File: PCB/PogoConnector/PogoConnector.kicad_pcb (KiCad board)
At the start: 2 copper layers, 7 x 20 mm, 7 parts, among them J1 PogoPinPad, J2 Conn_01x06, J3 PogoPinPad, J4 PogoPinPad, U1 PogoPin, U2 PogoPin, U3 PogoPin

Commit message: Update PCB
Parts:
- J2: footprint Connector_PinHeader_2.54mm:PinHeader_1x06_P2.54mm_Vertical -> CustomFootprints:Connector_PinHeader_2.54mm_Vertical
- moved J2 6.35 mm to (126.8, 95.0)
- moved J1 0.23 mm to (129.8, 96.5)
- moved J3 0.23 mm to (129.8, 99.5)
- moved J4 0.23 mm to (129.8, 102.5)
- moved U1 0.23 mm to (129.8, 87.5)
- moved U2 0.23 mm to (129.8, 90.5)
- moved U3 0.23 mm to (129.8, 93.5)
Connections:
- J1 pad 1: /Data1 -> GND
- J2 pad 1: GND -> +5V
- J2 pad 2: +5V -> /Data1
- J2 pad 3: /Data2 -> GND
- J2 pad 4: /Data1 -> GND
- J2 pad 5: +5V -> /Data2
- J2 pad 6: GND -> +5V
- J3 pad 1: +5V -> /Data2
- J4 pad 1: GND -> +5V
- U1 pad 1: GND -> +5V
- U2 pad 1: +5V -> /Data1
- U3 pad 1: /Data2 -> GND
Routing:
- net GND: track 7.45 -> 6.39 mm
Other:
- outline, holes or cut-outs redrawn

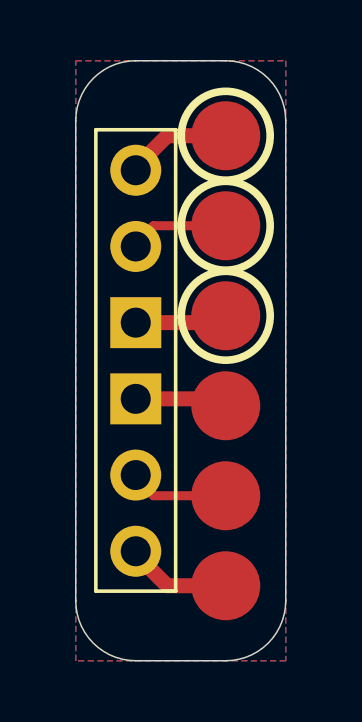
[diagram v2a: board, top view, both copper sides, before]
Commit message: Add hall sensor shield
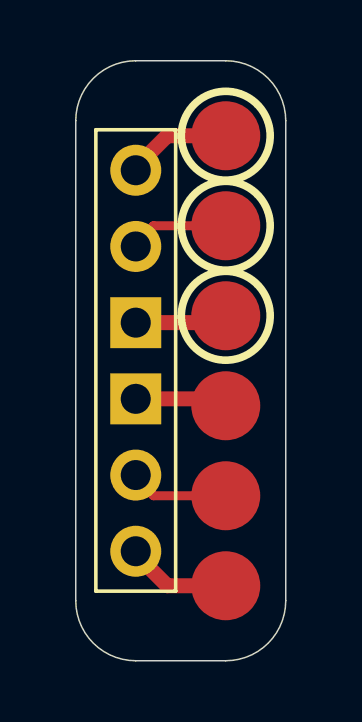
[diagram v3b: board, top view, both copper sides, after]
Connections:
- J1 pad 1: GND -> GND2
- J2 pad 4: GND -> GND2
- J2 pad 6: +5V -> +5V2
- J4 pad 1: +5V -> +5V2
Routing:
- net +5V2: track 0.00 -> 3.58 mm
- net +5V: track 7.15 -> 3.58 mm
- net GND: track 6.39 -> 3.20 mm
- net GND2: track 0.00 -> 3.20 mm
- removed copper zone on F.Cu, net +5V
- removed copper zone on B.Cu, net GND
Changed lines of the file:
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@@
 	(net 3 "/Data2")
 	(net 4 "+5V")
+	(net 5 "GND2")
+	(net 6 "+5V2")
 	(footprint "CustomFootprints:Connector_PinHeader_2.54mm_Vertical"
 		(layer "F.Cu")
@@
 			)
 			(remove_unused_layers no)
-			(net 1 "GND")
+			(net 5 "GND2")
 			(pinfunction "Pin_4")
 			(pintype "passive")
@@
 			)
 			(remove_unused_layers no)
-			(net 4 "+5V")
+			(net 6 "+5V2")
 			(pinfunction "Pin_6")
 			(pintype "passive")
@@
 			(size 2.3 2.3)
 			(layers "F.Cu" "F.Paste" "F.Mask")
-			(net 1 "GND")
+			(net 5 "GND2")
 			(pinfunction "Pin_1")
 			(pintype "passive")
@@
 			(size 2.3 2.3)
 			(layers "F.Cu" "F.Paste" "F.Mask")
-			(net 4 "+5V")
+			(net 6 "+5V2")
 			(pinfunction "Pin_1")
 			(pintype "passive")
@@
 	)
 	(segment
+		(start 127.36 90.5)
+		(end 126.67 91.19)
+		(width 0.3)
+		(layer "F.Cu")
+		(net 2)
+	)
+	(segment
+		(start 129.77 90.5)
+		(end 127.36 90.5)
+		(width 0.3)
+		(layer "F.Cu")
+		(net 2)
+	)
+	(segment
+		(start 129.77 99.5)
+		(end 127.36 99.5)
+		(width 0.3)
+		(layer "F.Cu")
+		(net 3)
+	)
+	(segment
+		(start 127.36 99.5)
+		(end 126.67 98.81)
+		(width 0.3)
+		(layer "F.Cu")
+		(net 3)
+	)
+	(segment
+		(start 129.77 87.5)
+		(end 127.82 87.5)
+		(width 0.5)
+		(layer "F.Cu")
+		(net 4)
+	)
+	(segment
+		(start 127.82 87.5)
+		(end 126.67 88.65)
+		(width 0.5)
+		(layer "F.Cu")
+		(net 4)
+	)
+	(segment
 		(start 126.67 96.27)
 		(end 129.54 96.27)
 		(width 0.5)
 		(layer "F.Cu")
-		(net 1)
+		(net 5)
 	)
 	(segment
@@
 		(width 0.5)
 		(layer "F.Cu")
-		(net 1)
-	)
-	(segment
-		(start 127.36 90.5)
-		(end 126.67 91.19)
-		(width 0.3)
-		(layer "F.Cu")
-		(net 2)
-	)
-	(segment
-		(start 129.77 90.5)
-		(end 127.36 90.5)
-		(width 0.3)
-		(layer "F.Cu")
-		(net 2)
-	)
-	(segment
-		(start 129.77 99.5)
-		(end 127.36 99.5)
-		(width 0.3)
-		(layer "F.Cu")
-		(net 3)
-	)
-	(segment
-		(start 127.36 99.5)
-		(end 126.67 98.81)
-		(width 0.3)
-		(layer "F.Cu")
-		(net 3)
+		(net 5)
 	)
 	(segment
@@
 		(width 0.5)
 		(layer "F.Cu")
-		(net 4)
-	)
-	(segment
-		(start 129.77 87.5)
-		(end 127.82 87.5)
-		(width 0.5)
-		(layer "F.Cu")
-		(net 4)
-	)
-	(segment
-		(start 127.82 87.5)
-		(end 126.67 88.65)
-		(width 0.5)
-		(layer "F.Cu")
-		(net 4)
+		(net 6)
 	)
 	(segment
@@
 		(width 0.5)
 		(layer "F.Cu")
-		(net 4)
-	)
-	(zone
-		(net 4)
-		(net_name "+5V")
-		(layer "F.Cu")
-		(hatch edge 0.5)
-		(connect_pads yes
-			(clearance 0.5)
-		)
-		(min_thickness 0.25)
-		(filled_areas_thickness no)
-		(fill yes
-			(thermal_gap 0.5)
-			(thermal_bridge_width 0.5)
-		)
-		(polygon
-			(pts
-				(xy 124.77 85) (xy 131.77 85) (xy 131.77 105) (xy 124.77 105)
-			)
-		)
-	)
-	(zone
-		(net 1)
-		(net_name "GND")
-		(layer "B.Cu")
-		(hatch edge 0.5)
-		(priority 1)
-		(connect_pads yes
-			(clearance 0.5)
-		)
-		(min_thickness 0.25)
-		(filled_areas_thickness no)
-		(fill yes
-			(thermal_gap 0.5)
-			(thermal_bridge_width 0.5)
-		)
-		(polygon
-			(pts
-				(xy 124.77 85) (xy 131.77 85) (xy 131.77 105) (xy 124.77 105)
-			)
-		)
+		(net 6)
 	)
 )

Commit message: Add smart cube panel
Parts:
- added REF**: Tab, PCM_kikit:Tab, F.Cu at (124.6, 95.0)
- added REF**: Tab, PCM_kikit:Tab, F.Cu at (132.0, 95.0)
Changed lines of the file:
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@@
 	(net 5 "GND2")
 	(net 6 "+5V2")
+	(footprint "PCM_kikit:Tab"
+		(layer "F.Cu")
+		(at 124.57 95)
+		(descr "A symbol representing annotation for tab placement")
+		(property "Reference" "REF**"
+			(at -0.25 -2 0)
+			(layer "F.SilkS")
+			(hide yes)
+			(effects
+				(font
+					(size 1 1)
+					(thickness 0.15)
+				)
+			)
+		)
+		(property "Value" "Tab"
+			(at -3 -1 0)
+			(layer "Dwgs.User")
+			(effects
+				(font
+					(size 1.2 1.2)
+					(thickness 0.2)
+				)
+			)
+		)
+		(property "Footprint" "PCM_kikit:Tab"
+			(at 0 0 0)
+			(layer "F.Fab")
+			(hide yes)
+			(effects
+				(font
+					(size 1.27 1.27)
+					(thickness 0.15)
+				)
+			)
+		)
+		(property "Datasheet" ""
+			(at 0 0 0)
+			(layer "F.Fab")
+			(hide yes)
+			(effects
+				(font
+					(size 1.27 1.27)
+					(thickness 0.15)
+				)
+			)
+		)
+		(property "Description" ""
+			(at 0 0 0)
+			(layer "F.Fab")
+			(hide yes)
+			(effects
+				(font
+					(size 1.27 1.27)
+					(thickness 0.15)
+				)
+			)
+		)
+		(attr board_only exclude_from_pos_files exclude_from_bom allow_missing_courtyard)
+		(fp_line
+			(start 0 0)
+			(end -3 0)
+			(stroke
+				(width 0.3)
+				(type solid)
+			)
+			(layer "Dwgs.User")
+		)
+		(fp_line
+			(start 0 0)
+			(end -1 -1)
+			(stroke
+				(width 0.3)
+				(type solid)
+			)
+			(layer "Dwgs.User")
+		)
+		(fp_line
+			(start 0 0)
+			(end -1 1)
+			(stroke
+				(width 0.3)
+				(type solid)
+			)
+			(layer "Dwgs.User")
+		)
+		(fp_line
+			(start 0 1)
+			(end 0 -1)
+			(stroke
+				(width 0.3)
+				(type solid)
+			)
+			(layer "Dwgs.User")
+		)
+		(fp_text user "KIKIT: width: 5mm"
+			(at -5.5 0 90)
+			(layer "Dwgs.User")
+			(effects
+				(font
+					(size 1 1)
+					(thickness 0.15)
+				)
+			)
+		)
+	)
 	(footprint "CustomFootprints:Connector_PinHeader_2.54mm_Vertical"
 		(layer "F.Cu")
@@
 			)
 		)
+	)
+	(footprint "PCM_kikit:Tab"
+		(layer "F.Cu")
+		(at 131.97 95 180)
+		(descr "A symbol representing annotation for tab placement")
+		(property "Reference" "REF**"
+			(at -0.25 -2 0)
+			(layer "F.SilkS")
+			(hide yes)
+			(effects
+				(font
+					(size 1 1)
+					(thickness 0.15)
+				)
+			)
+		)
+		(property "Value" "Tab"
+			(at -3 -1 0)
+			(layer "Dwgs.User")
+			(effects
+				(font
+					(size 1.2 1.2)
+					(thickness 0.2)
+				)
+			)
+		)
+		(property "Footprint" "PCM_kikit:Tab"
+			(at 0 0 0)
+			(layer "F.Fab")
+			(hide yes)
+			(effects
+				(font
+					(size 1.27 1.27)
+					(thickness 0.15)
+				)
+			)
+		)
+		(property "Datasheet" ""
+			(at 0 0 0)
+			(layer "F.Fab")
+			(hide yes)
+			(effects
+				(font
+					(size 1.27 1.27)
+					(thickness 0.15)
+				)
+			)
+		)
+		(property "Description" ""
+			(at 0 0 0)
+			(layer "F.Fab")
+			(hide yes)
+			(effects
+				(font
+					(size 1.27 1.27)
+					(thickness 0.15)
+				)
+			)
+		)
+		(attr board_only exclude_from_pos_files exclude_from_bom allow_missing_courtyard)
+		(fp_line
+			(start 0 1)
+			(end 0 -1)
+			(stroke
+				(width 0.3)
+				(type solid)
+			)
+			(layer "Dwgs.User")
+		)
+		(fp_line
+			(start 0 0)
+			(end -1 1)
+			(stroke
+				(width 0.3)
+				(type solid)
+			)
+			(layer "Dwgs.User")
+		)
+		(fp_line
+			(start 0 0)
+			(end -1 -1)
+			(stroke
+				(width 0.3)
+				(type solid)
+			)
+			(layer "Dwgs.User")
+		)
+		(fp_line
+			(start 0 0)
+			(end -3 0)
+			(stroke
+				(width 0.3)
+				(type solid)
+			)
+			(layer "Dwgs.User")
+		)
+		(fp_text user "KIKIT: width: 5mm"
+			(at -5.5 0 90)
+			(layer "Dwgs.User")
+			(effects
+				(font
+					(size 1 1)
+					(thickness 0.15)
+				)
+			)
+		)

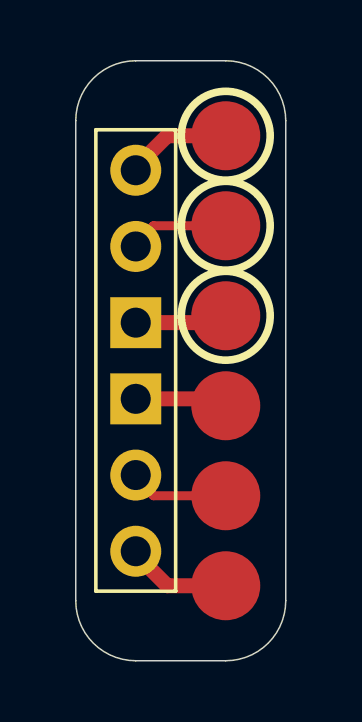
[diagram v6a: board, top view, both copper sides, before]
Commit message: Finish module, power supply and connector design, panel is wip
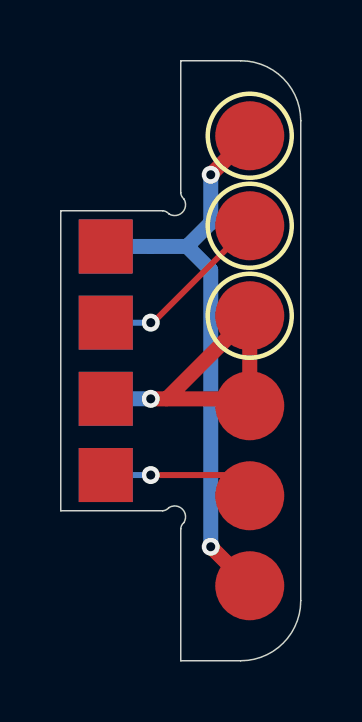
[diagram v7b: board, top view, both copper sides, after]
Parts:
- J2: footprint CustomFootprints:Connector_PinHeader_2.54mm_Vertical -> CustomFootprints:01x04_PinPads; moved to B.Cu
- moved J2 1.00 mm to (125.8, 95.0), turned to -90 degrees
- moved J1 0.80 mm to (130.6, 96.5)
- moved J3 0.80 mm to (130.6, 99.5)
- moved J4 0.80 mm to (130.6, 102.5)
- moved U1 0.80 mm to (130.6, 87.5)
- moved U2 0.80 mm to (130.6, 90.5)
- moved U3 0.80 mm to (130.6, 93.5)
- moved REF** 0.50 mm to (124.1, 95.0)
- moved REF** 0.50 mm to (132.5, 95.0)
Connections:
- J1 pad 1: GND2 -> GND
- J2 pad 4: GND2 -> /Data2
- J4 pad 1: +5V2 -> +5V
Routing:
- net +5V: track 3.58 -> 19.4 mm, vias 0 -> 2
- net GND: track 3.20 -> 11.8 mm, vias 0 -> 1
- net +5V2: track 3.58 -> 0.00 mm
- net GND2: track 3.20 -> 0.00 mm
- net /Data1: track 3.39 -> 6.14 mm, vias 0 -> 1
- net /Data2: track 3.39 -> 5.09 mm, vias 0 -> 1
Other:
- board size 7 x 20 mm -> 8 x 20 mm
- board text added: "+"
- board text added: "-"
- board text added: "1"
- board text added: "2"
- board text added: "5V"
- board text added: "D1"
- board text added: "D2"
- board text added: "GND"

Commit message: Finish panel script
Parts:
- added J5: Conn_01x06, CustomFootprints:01x04_PinPads_Single, B.Cu at (129.2, 95.0)
- J2: footprint CustomFootprints:01x04_PinPads -> CustomFootprints:01x04_PinPads_Single
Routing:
- net GND: track 11.8 -> 12.7 mm
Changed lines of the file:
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@@
 		)
 	)
-	(footprint "CustomFootprints:01x04_PinPads"
+	(footprint "CustomFootprints:01x04_PinPads_Single"
+		(layer "B.Cu")
+		(at 129.17 95 -90)
+		(property "Reference" "J5"
+			(at 0 0.5 90)
+			(unlocked yes)
+			(layer "B.SilkS")
+			(hide yes)
+			(effects
+				(font
+					(size 1 1)
+					(thickness 0.1)
+				)
+				(justify mirror)
+			)
+		)
+		(property "Value" "Conn_01x06"
+			(at 0 -1 90)
+			(unlocked yes)
+			(layer "B.Fab")
+			(effects
+				(font
+					(size 1 1)
+					(thickness 0.15)
+				)
+				(justify mirror)
+			)
+		)
+		(property "Footprint" "CustomFootprints:01x04_PinPads_Single"
+			(at 0 0 90)
+			(unlocked yes)
+			(layer "B.Fab")
+			(hide yes)
+			(effects
+				(font
+					(size 1 1)
+					(thickness 0.15)
+				)
+				(justify mirror)
+			)
+		)
+		(property "Datasheet" ""
+			(at 0 0 90)
+			(unlocked yes)
+			(layer "B.Fab")
+			(hide yes)
+			(effects
+				(font
+					(size 1 1)
+					(thickness 0.15)
+				)
+				(justify mirror)
+			)
+		)
+		(property "Description" "Generic connector, single row, 01x04, script generated (kicad-library-utils/schlib/autogen/connector/)"
+			(at 0 0 90)
+			(unlocked yes)
+			(layer "B.Fab")
+			(hide yes)
+			(effects
+				(font
+					(size 1 1)
+					(thickness 0.15)
+				)
+				(justify mirror)
+			)
+		)
+		(property ki_fp_filters "Connector*:*_1x??_*")
+		(sheetname "Root")
+		(sheetfile "PogoConnector.kicad_sch")
+		(attr smd exclude_from_bom dnp)
+		(fp_text user "${REFERENCE}"
+			(at 0 -2.5 90)
+			(unlocked yes)
+			(layer "B.Fab")
+			(effects
+				(font
+					(size 1 1)
+					(thickness 0.15)
+				)
+				(justify mirror)
+			)
+		)
+		(fp_text user "${REFERENCE}"
+			(at 0 -2.5 90)
+			(unlocked yes)
+			(layer "B.Fab")
+			(effects
+				(font
+					(size 1 1)
+					(thickness 0.15)
+				)
+				(justify mirror)
+			)
+		)
+		(fp_text user "REF**"
+			(at 0 -12.8 90)
+			(layer "B.Fab")
+			(effects
+				(font
+					(size 1 1)
+					(thickness 0.15)
+				)
+				(justify mirror)
+			)
+		)
+		(fp_text user "${REFERENCE}"
+			(at 0 -2.5 90)
+			(unlocked yes)
+			(layer "B.Fab")
+			(effects
+				(font
+					(size 1 1)
+					(thickness 0.15)
+				)
+				(justify mirror)
+			)
+		)
+		(pad "1" smd rect
+			(at -3.810008 0 270)
+			(size 1.8 1.8)
+			(layers "B.Cu" "B.Paste" "B.Mask")
+			(net 4 "+5V")
+			(pinfunction "Pin_1")
+			(pintype "passive")
+		)
+		(pad "2" smd rect
+			(at -1.270003 0 270)
+			(size 1.8 1.8)
+			(layers "B.Cu" "B.Paste" "B.Mask")
+			(net 4 "+5V")
+			(pinfunction "Pin_2")
+			(pintype "passive")
+		)
+		(pad "3" smd rect
+			(at 1.270003 0 270)
+			(size 1.8 1.8)
+			(layers "B.Cu" "B.Paste" "B.Mask")
+			(net 4 "+5V")
+			(pinfunction "Pin_3")
+			(pintype "passive")
+		)
+		(pad "4" smd rect
+			(at 3.810008 0 270)
+			(size 1.8 1.8)
+			(layers "B.Cu" "B.Paste" "B.Mask")
+			(net 4 "+5V")
+			(pinfunction "Pin_4")
+			(pintype "passive")
+		)
+	)
+	(footprint "CustomFootprints:01x04_PinPads_Single"
 		(layer "B.Cu")
 		(at 125.77 95 -90)
@@
 		)
 		(property "Value" "Conn_01x06"
-			(at 0.429997 -0.8 90)
-			(unlocked yes)
-			(layer "B.Fab")
-			(effects
-				(font
-					(size 1 1)
-					(thickness 0.15)
-				)
-				(justify mirror)
-			)
-		)
-		(property "Footprint" "CustomFootprints:01x04_PinPads"
+			(at 0 -1 90)
+			(unlocked yes)
+			(layer "B.Fab")
+			(effects
+				(font
+					(size 1 1)
+					(thickness 0.15)
+				)
+				(justify mirror)
+			)
+		)
+		(property "Footprint" "CustomFootprints:01x04_PinPads_Single"
 			(at 0 0 90)
 			(unlocked yes)
@@
 		(sheetname "Root")
 		(sheetfile "PogoConnector.kicad_sch")
-		(attr smd dnp)
+		(attr smd exclude_from_bom dnp)
+		(fp_text user "REF**"
+			(at 0 -12.8 90)
+			(layer "B.Fab")
+			(effects
+				(font
+					(size 1 1)
+					(thickness 0.15)
+				)
+				(justify mirror)
+			)
+		)
 		(fp_text user "${REFERENCE}"
 			(at 0 -2.5 90)
@@
 			)
 		)
-		(fp_text user "REF**"
-			(at 0 -12.8 90)
-			(layer "B.Fab")
-			(effects
-				(font
-					(size 1 1)
-					(thickness 0.15)
-				)
-				(justify mirror)
-			)
-		)
 		(fp_text user "${REFERENCE}"
 			(at 0 -2.5 90)
@@
 			)
 		)
-		(pad "" smd rect
-			(at -3.81 0 270)
-			(size 1.8 1.8)
-			(layers "F.Cu" "F.Paste" "F.Mask")
-		)
-		(pad "" smd rect
-			(at -1.27 0 270)
-			(size 1.8 1.8)
-			(layers "F.Cu" "F.Paste" "F.Mask")
-		)
-		(pad "" smd rect
-			(at 1.27 0 270)
-			(size 1.8 1.8)
-			(layers "F.Cu" "F.Paste" "F.Mask")
-		)
-		(pad "" smd rect
-			(at 3.81 0 270)
-			(size 1.8 1.8)
-			(layers "F.Cu" "F.Paste" "F.Mask")
+		(fp_text user "${REFERENCE}"
+			(at 0 -2.5 90)
+			(unlocked yes)
+			(layer "B.Fab")
+			(effects
+				(font
+					(size 1 1)
+					(thickness 0.15)
+				)
+				(justify mirror)
+			)
 		)
 		(pad "1" smd rect
@@
 	)
 	(gr_text "+"
-		(at 128.07 91.1 -0)
+		(at 127.67 91.1 -0)
 		(layer "B.SilkS")
 		(effects
@@
 	)
 	(gr_text "1"
-		(at 128.07 93.7 -0)
+		(at 127.67 93.7 -0)
 		(layer "B.SilkS")
 		(effects
@@
 	)
 	(gr_text "-"
-		(at 128.07 96.2 -0)
+		(at 127.67 96.2 -0)
 		(layer "B.SilkS")
 		(effects
@@
 	)
 	(gr_text "2"
-		(at 128.17 98.8 -0)
+		(at 127.77 98.8 -0)
 		(layer "B.SilkS")
 		(effects
@@
 	)
 	(segment
-		(start 130.57 93.5)
-		(end 127.799997 96.270003)
-		(width 0.5)
-		(layer "F.Cu")
-		(net 1)
-	)
-	(segment
-		(start 130.340003 96.270003)
-		(end 130.57 96.5)
+		(start 127.77 96.3)
+		(end 126.97 96.3)
 		(width 0.5)
 		(layer "F.Cu")
@@
 	)
 	(segment
-		(start 127.27 96.270003)
-		(end 130.340003 96.270003)
+		(start 126.97 96.3)
+		(end 130.37 96.3)
 		(width 0.5)
 		(layer "F.Cu")
 		(net 1)
 	)
+	(segment
+		(start 130.57 93.5)
+		(end 127.77 96.3)
+		(width 0.5)
+		(layer "F.Cu")
+		(net 1)
+	)
+	(segment
+		(start 130.37 96.3)
+		(end 130.57 96.5)
+		(width 0.5)
+		(layer "F.Cu")
+		(net 1)
+	)
 	(via
-		(at 127.27 96.270003)
+		(at 126.97 96.3)
 		(size 0.6)
 		(drill 0.3)
@@
 	)
 	(segment
-		(start 125.77 96.270003)
-		(end 127.27 96.270003)
+		(start 126.97 96.3)
+		(end 126.940003 96.270003)
 		(width 0.5)
 		(layer "B.Cu")
@@
 	)
 	(segment
-		(start 127.27 93.729997)
+		(start 126.940003 96.270003)
+		(end 125.77 96.270003)
+		(width 0.5)
+		(layer "B.Cu")
+		(net 1)
+	)
+	(segment
+		(start 126.97 93.729997)
 		(end 127.340003 93.729997)
 		(width 0.2)
@@
 	)
 	(via
-		(at 127.27 93.729997)
+		(at 126.97 93.729997)
 		(size 0.6)
 		(drill 0.3)
@@
 	(segment
 		(start 125.77 93.729997)
-		(end 127.27 93.729997)
+		(end 126.97 93.729997)
 		(width 0.2)
 		(layer "B.Cu")
@@
 	)
 	(segment
-		(start 127.27 98.810008)
-		(end 129.880008 98.810008)
-		(width 0.2)
-		(layer "F.Cu")
-		(net 3)
-	)
-	(segment
 		(start 129.880008 98.810008)
 		(end 130.57 99.5)
@@
 		(net 3)
 	)
+	(segment
+		(start 126.97 98.810008)
+		(end 129.880008 98.810008)
+		(width 0.2)
+		(layer "F.Cu")
+		(net 3)
+	)
 	(via
-		(at 127.27 98.810008)
+		(at 126.97 98.810008)
 		(size 0.6)
 		(drill 0.3)
@@
 	(segment
 		(start 125.77 98.810008)
-		(end 127.27 98.810008)
+		(end 126.97 98.810008)
 		(width 0.2)
 		(layer "B.Cu")
